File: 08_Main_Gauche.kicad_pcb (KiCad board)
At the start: 2 copper layers, 150 x 130 mm, 67 parts, among them J1 Conn_01x04, SW1 MX_1u, SW10 MX_1u, SW11 SW_Push_LED, SW12 MX_1u, SW13 K1-1506SN-01, SW14 MX_1u, SW15 MX_1u, SW16 MX_1u, SW17 MX_1u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

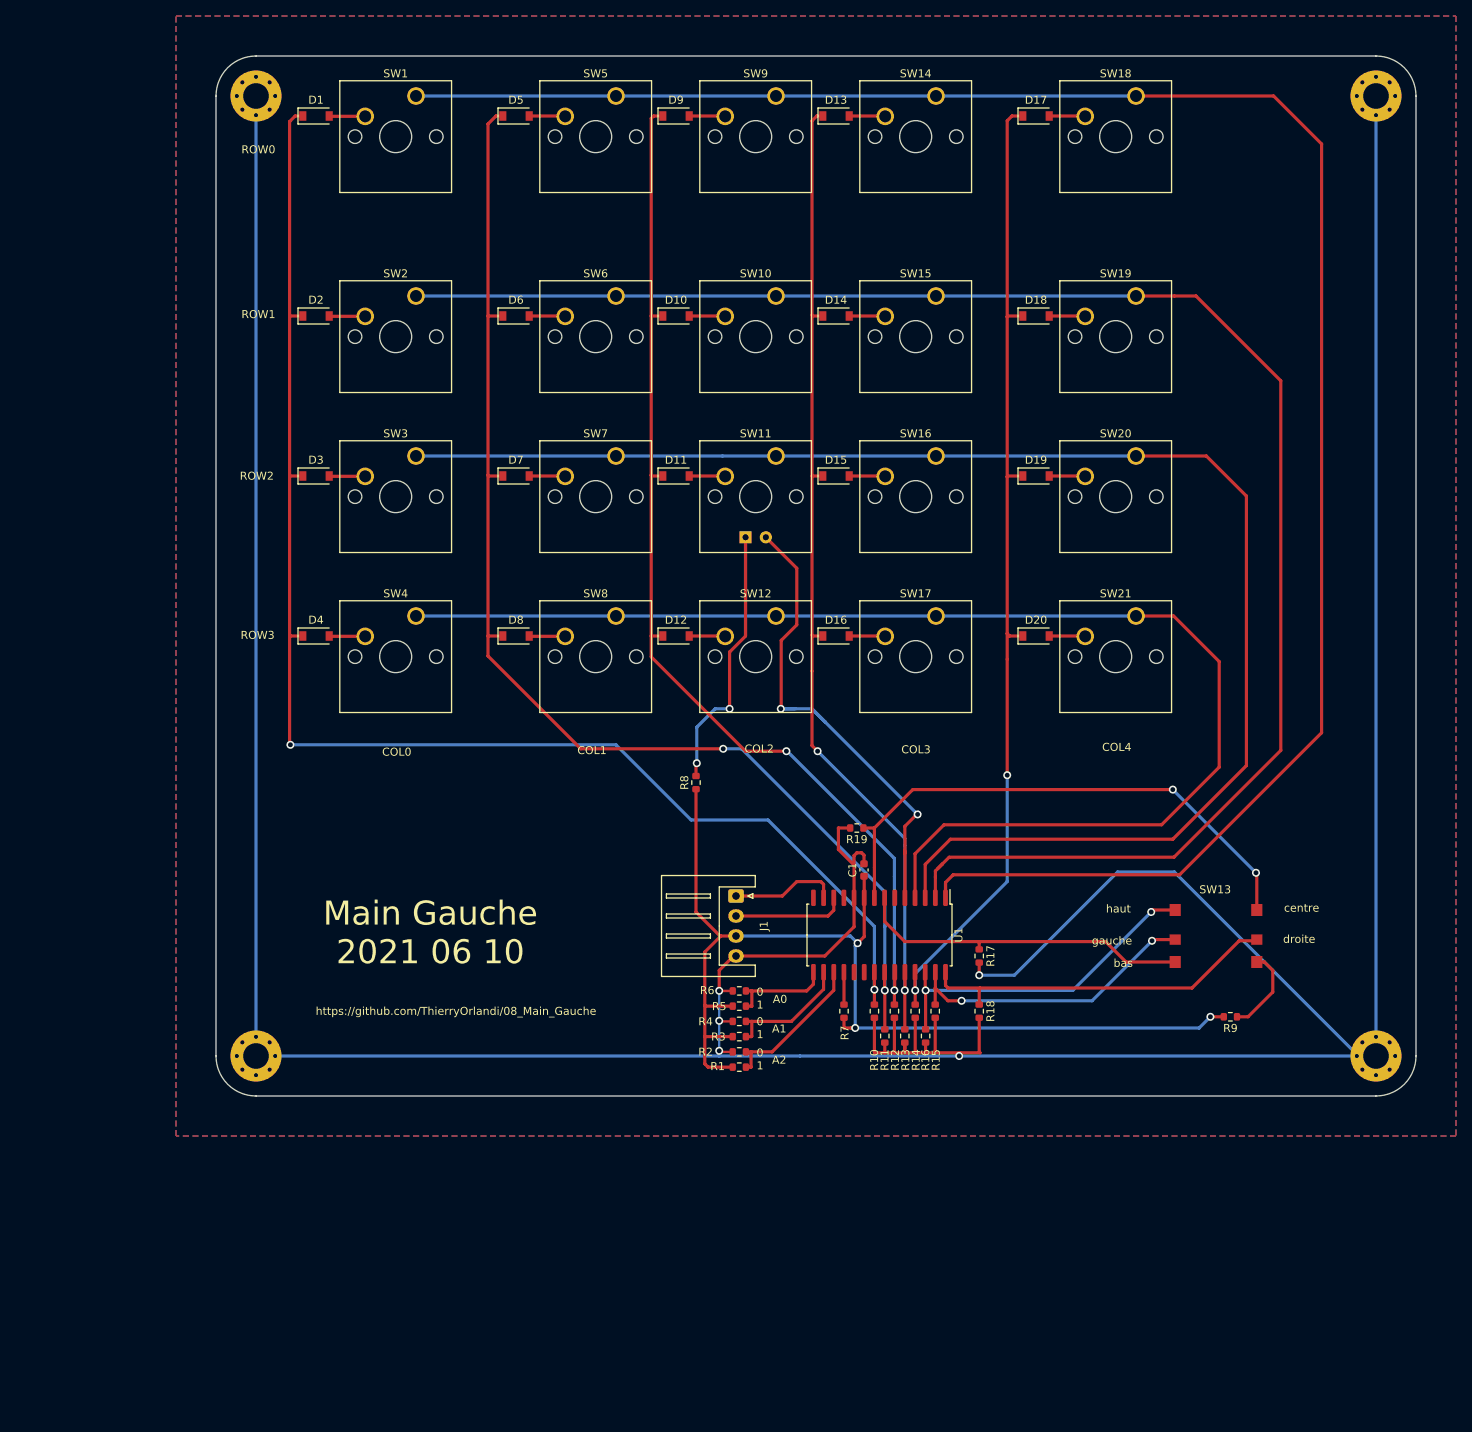
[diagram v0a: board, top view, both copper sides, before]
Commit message: correction schema et routage
changement symbole et empreinte de arduino micro socket
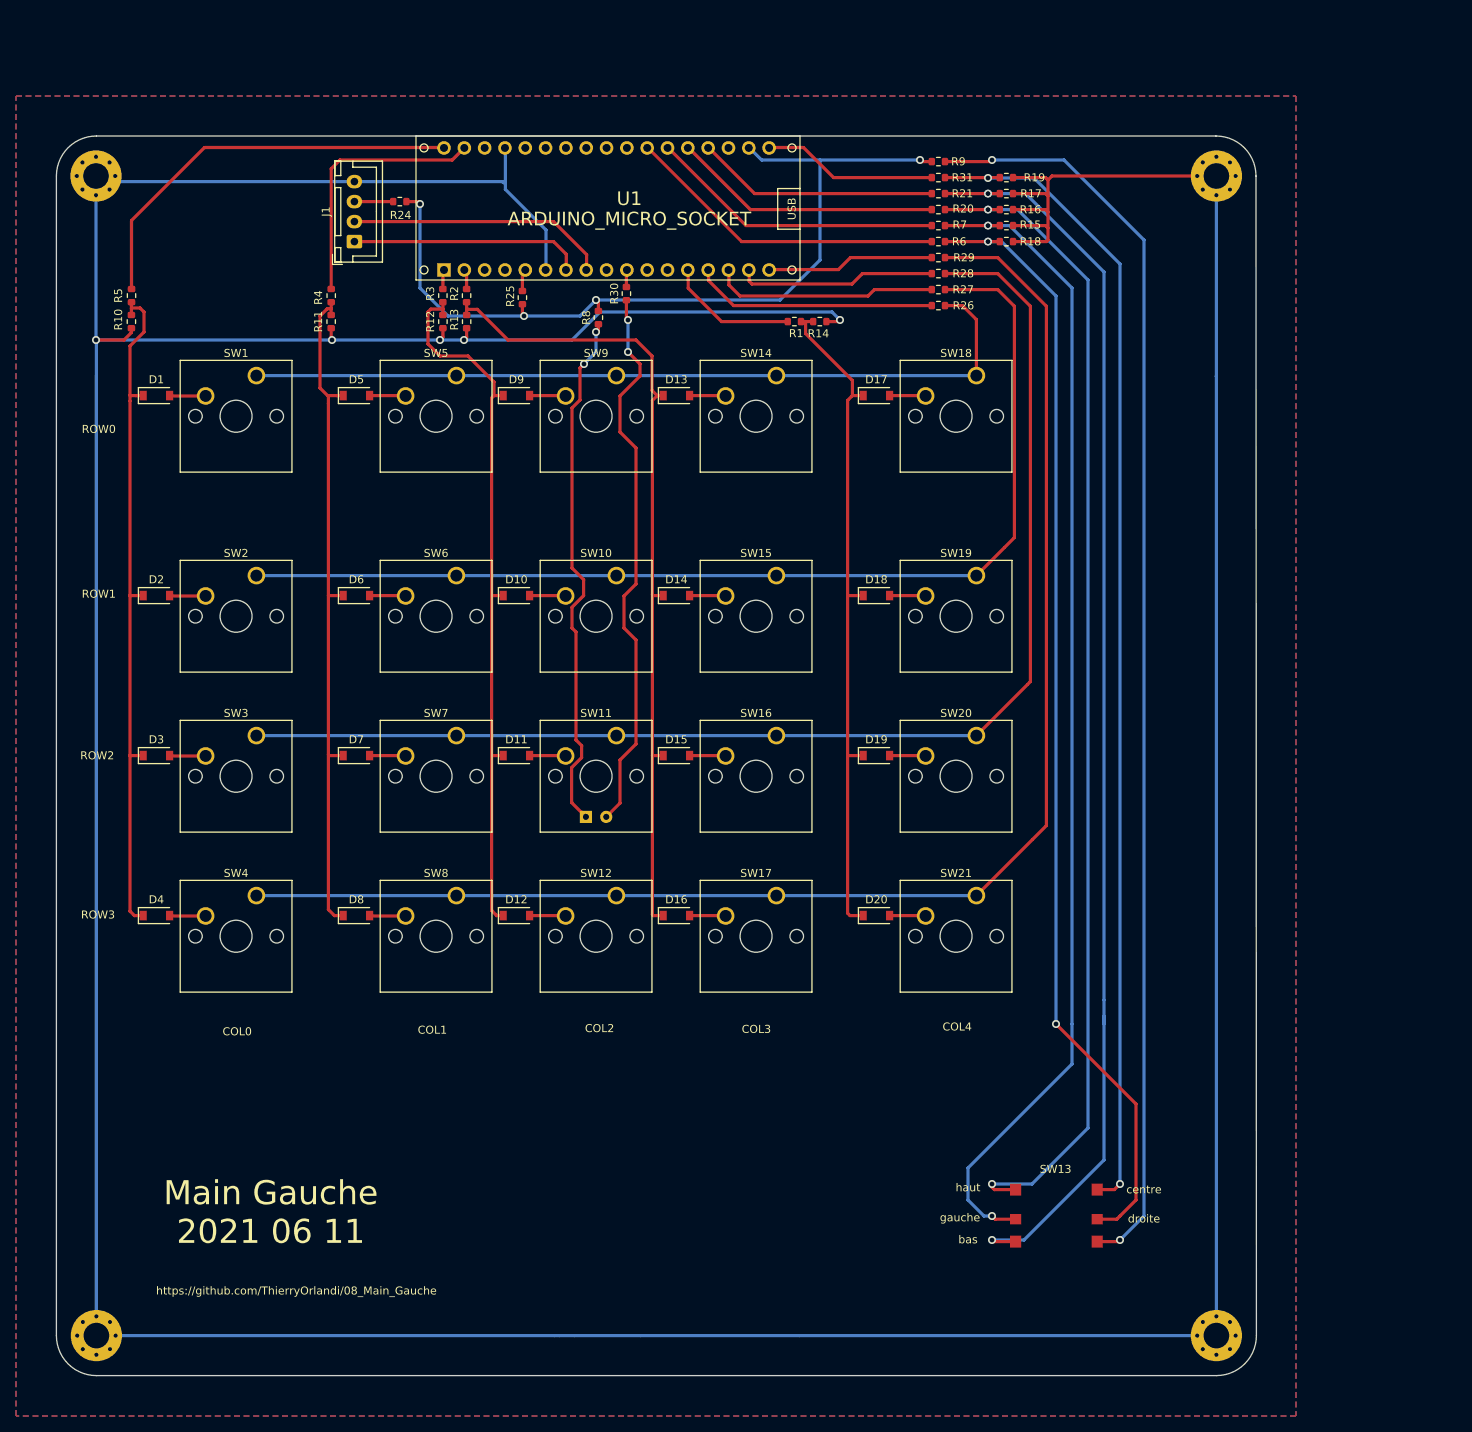
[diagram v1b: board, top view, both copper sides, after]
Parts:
- removed C1: 100nF, Capacitor_SMD:C_0603_1608Metric
- added R20: 0, Resistor_SMD:R_0603_1608Metric, F.Cu at (130.3, 34.2)
- added R21: 0, Resistor_SMD:R_0603_1608Metric, F.Cu at (130.3, 32.2)
- added R24: 0, Resistor_SMD:R_0603_1608Metric, F.Cu at (63.0, 33.2)
- added R25: 100k, Resistor_SMD:R_0603_1608Metric, F.Cu at (78.3, 45.2)
- added R26: 0, Resistor_SMD:R_0603_1608Metric, F.Cu at (130.3, 46.2)
- added R27: 0, Resistor_SMD:R_0603_1608Metric, F.Cu at (130.3, 44.2)
- added R28: 0, Resistor_SMD:R_0603_1608Metric, F.Cu at (130.3, 42.2)
- added R29: 0, Resistor_SMD:R_0603_1608Metric, F.Cu at (130.3, 40.2)
- added R30: 0, Resistor_SMD:R_0603_1608Metric, F.Cu at (91.3, 44.7)
- added R31: 0, Resistor_SMD:R_0603_1608Metric, F.Cu at (130.3, 30.2)
- J1: footprint Connector_JST:JST_XH_S4B-XH-A_1x04_P2.50mm_Horizontal -> Connector_JST:JST_XH_B4B-XH-A_1x04_P2.50mm_Vertical
- R1, R2, R3, R4, R5, R6, R7: value 100k -> 0
- U1: value MCP23017_SO -> ARDUINO_MICRO_SOCKET; footprint Package_SO:SOIC-28W_7.5x17.9mm_P1.27mm -> Chimere:ARDUINO_MICRO_SCKT
- moved R10 126.7 mm to (29.4, 48.2)
- moved R5 116.9 mm to (29.4, 45.0), turned to 90 degrees
- moved R11 113.0 mm to (54.4, 48.2)
- moved R9 113.0 mm to (130.3, 28.2)
- moved R13 104.8 mm to (71.3, 48.2)
- moved R4 104.1 mm to (54.4, 45.0), turned to 90 degrees
- moved R16 103.8 mm to (138.8, 34.2), turned to 0 degrees
- moved R12 103.0 mm to (68.4, 48.2)
- moved R2 100.5 mm to (71.3, 45.0), turned to 90 degrees
- moved U1 100.3 mm to (65.0, 43.0), turned to 0 degrees
- moved R3 99.8 mm to (68.4, 45.0), turned to 90 degrees
- moved R7 98.9 mm to (130.3, 36.2), turned to 180 degrees
- moved R15 98.6 mm to (138.8, 36.2), turned to 0 degrees
- moved R6 96.9 mm to (130.3, 38.2), turned to 180 degrees
- moved R18 96.3 mm to (138.8, 38.2), turned to 0 degrees
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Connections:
- J1 pad 3: 3V3 -> Net-(J1-Pad3)
- R1 pad 1: 3V3 -> COL4
- R2 pad 1: GND -> COL3
- R2 pad 2: Net-(R1-Pad2) -> Net-(R2-Pad2)
- R3 pad 1: 3V3 -> COL2
- R4 pad 1: GND -> COL1
- R4 pad 2: Net-(R3-Pad2) -> Net-(R4-Pad2)
- R5 pad 1: 3V3 -> COL0
- R6 pad 1: GND -> droite
- R6 pad 2: Net-(R5-Pad2) -> Net-(R6-Pad2)
- R7 pad 1: 3V3 -> gauche
- U1 pad 1: ROW0 -> Net-(R3-Pad2)
- U1 pad 10: GND -> Net-(R30-Pad1)
- U1 pad 12: SCL -> Net-(U1-Pad12)
- U1 pad 13: SDA -> Net-(R1-Pad2)
- U1 pad 15: Net-(R5-Pad2) -> Net-(R27-Pad1)
- U1 pad 16: Net-(R3-Pad2) -> Net-(R28-Pad1)
- U1 pad 17: Net-(R1-Pad2) -> Net-(R29-Pad1)
- U1 pad 18: Net-(R7-Pad2) -> Net-(R31-Pad1)
- U1 pad 19: Net-(U1-Pad19) -> 3V3
- U1 pad 2: ROW1 -> Net-(R2-Pad2)
- U1 pad 21: COL0 -> Net-(R21-Pad2)
- U1 pad 22: COL1 -> Net-(R20-Pad2)
- U1 pad 23: COL2 -> Net-(R7-Pad2)
- U1 pad 24: COL3 -> Net-(R6-Pad2)
- U1 pad 25: COL4 -> Net-(U1-Pad25)
- U1 pad 26: haut -> Net-(U1-Pad26)
- U1 pad 27: gauche -> Net-(U1-Pad27)
- U1 pad 28: droite -> Net-(U1-Pad28)
- U1 pad 3: ROW2 -> Net-(U1-Pad3)
- U1 pad 4: ROW3 -> Net-(U1-Pad4)
- U1 pad 5: led -> Net-(R25-Pad1)
- U1 pad 6: Net-(U1-Pad6) -> GND
- U1 pad 7: bas -> SDA
- U1 pad 8: centre -> SCL
- U1 pad 9: 3V3 -> Net-(U1-Pad9)
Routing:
- net GND: track 539.6 -> 779.1 mm
- net Net-(R9-Pad1): track 10.9 -> 158.3 mm, vias 0 -> 2
- net ROW0: track 246.0 -> 101.6 mm
- net bas: track 42.4 -> 158.6 mm, vias 0 -> 2
- net gauche: track 37.9 -> 146.9 mm
- net haut: track 42.5 -> 147.4 mm
- net droite: track 45.3 -> 141.2 mm, vias 0 -> 2
- net COL0: track 179.2 -> 86.8 mm, vias 2 -> 0
- net centre: track 68.8 -> 145.9 mm
- net ROW1: track 212.3 -> 135.2 mm
- net COL1: track 155.6 -> 86.7 mm, vias 2 -> 0
- net COL2: track 134.7 -> 89.8 mm, vias 2 -> 0
- net Net-(R6-Pad2): track 0.00 -> 40.4 mm
- net COL4: track 125.8 -> 85.6 mm, vias 2 -> 0
- net Net-(R5-Pad2): track 12.8 -> 51.5 mm
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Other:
- board size 150 x 130 mm -> 150 x 154.9 mm
- board text added: "Main Gauche 2021 06 11"
- board text removed: "0 1"
- board text removed: "A0"
- board text removed: "A1"
- board text removed: "A2"
- board text removed: "Main Gauche 2021 06 10"

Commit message: maj split librairies
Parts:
- SW11: footprint Chimere:SW_MX_LED -> Chimere_comps:SW_MX_LED
- SW13: footprint Chimere:K1-1506SN-01 -> Chimere_comps:K1-1506SN-01
- U1: footprint Chimere:ARDUINO_MICRO_SCKT -> Chimere_comps:ARDUINO_MICRO_SCKT
